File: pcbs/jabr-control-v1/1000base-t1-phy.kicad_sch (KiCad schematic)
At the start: 1 part, among them U6001 LAN8870

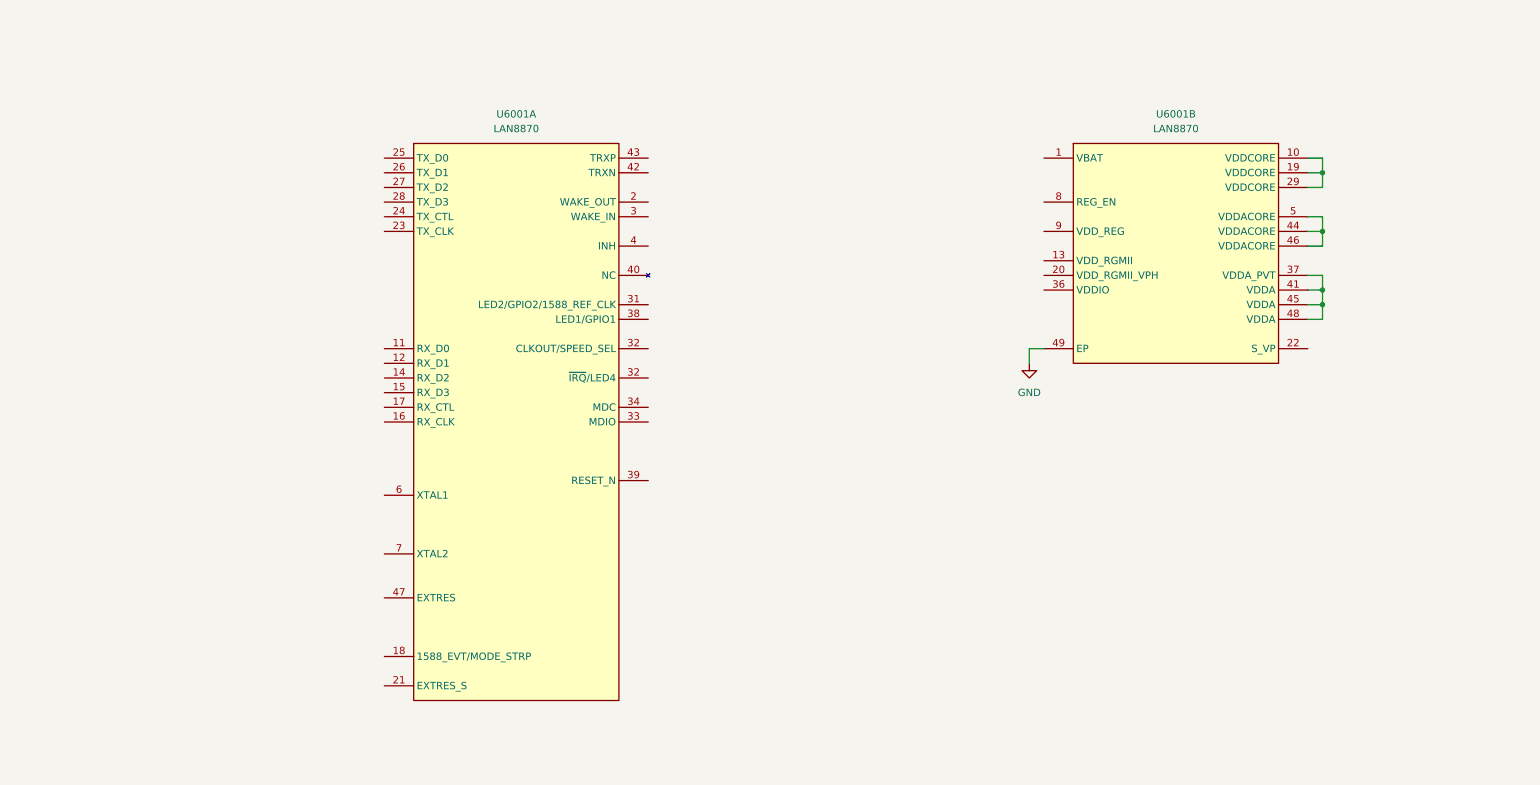
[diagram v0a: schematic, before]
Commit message: Added PCIe connections
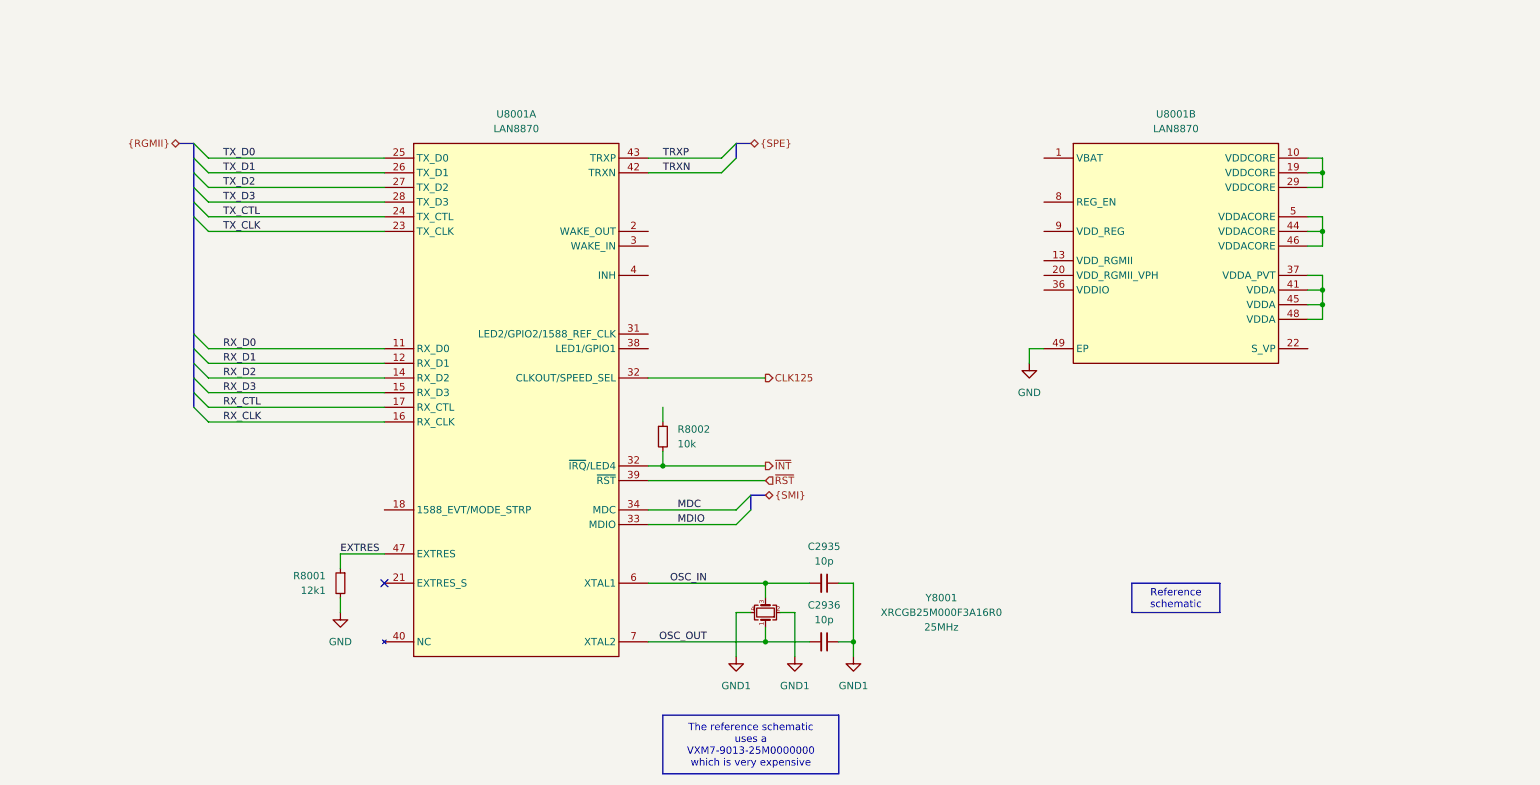
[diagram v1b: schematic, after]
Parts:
- added C2935, C2936: 10p, project_footprints:C_0402, symbol DEV:C_SMALL
- added R8001: 12k1, project_footprints:R_0402, symbol DEV:R_SMALL
- added R8002: 10k, project_footprints:R_0402, symbol DEV:R_SMALL
- added Y8001: XRCGB25M000F3A16R0, project_footprints:XRCGB25M000F3A16R0, symbol Device:Crystal_GND24_Small
- renumbered U6001 to U8001
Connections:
- net GND: now also R8001.2
- net RX_D0: now reaches U8001.11 (RX_D0)
- net RX_D1: now reaches U8001.12 (RX_D1)
- net RX_D2: now reaches U8001.14 (RX_D2)
- net RX_D3: now reaches U8001.15 (RX_D3)
- net RX_CLK: now reaches U8001.16 (RX_CLK)
- net RX_CTL: now reaches U8001.17 (RX_CTL)
- net TX_CLK: now reaches U8001.23 (TX_CLK)
- net TX_CTL: now reaches U8001.24 (TX_CTL)
- net TX_D0: now reaches U8001.25 (TX_D0)
- net TX_D1: now reaches U8001.26 (TX_D1)
- net TX_D2: now reaches U8001.27 (TX_D2)
- net TX_D3: now reaches U8001.28 (TX_D3)
- net ~{INT}: now reaches U8001.32 (~{IRQ}/LED4)
- net ~{INT}: now also R8002.2
- net MDIO: now reaches U8001.33 (MDIO)
- net MDC: now reaches U8001.34 (MDC)
- net ~{RST}: now reaches U8001.39 (~{RST})
- net TRXN: now reaches U8001.42 (TRXN)
- net TRXP: now reaches U8001.43 (TRXP)
- net EXTRES: now reaches U8001.47 (EXTRES)
- net EXTRES: now also R8001.1
- net OSC_IN: now reaches U8001.6 (XTAL1)
- net OSC_IN: now also C2935.2, Y8001.3
- net OSC_OUT: now reaches U8001.7 (XTAL2)
- net OSC_OUT: now also C2936.2, Y8001.1
- new net CLK125: U8001.32 (~{IRQ}/LED4)
- new net GND1: C2935.1, C2936.1, Y8001.2, Y8001.4
- no-connect marks 0 -> 1
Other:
- moved on the sheet: U8001A

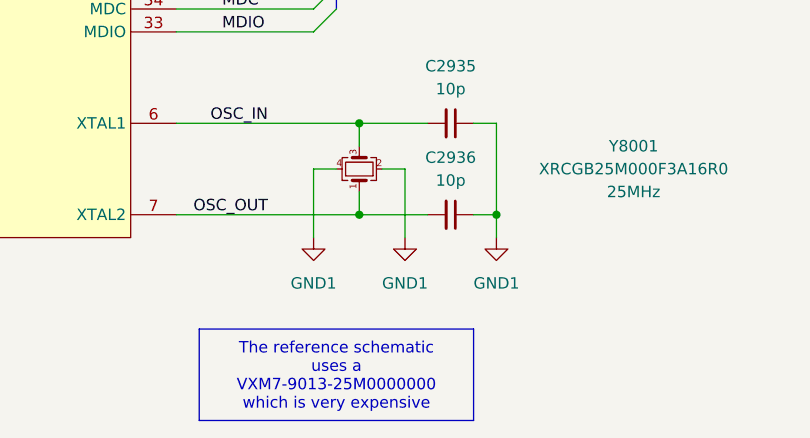
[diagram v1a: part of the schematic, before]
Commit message: Added power sheets
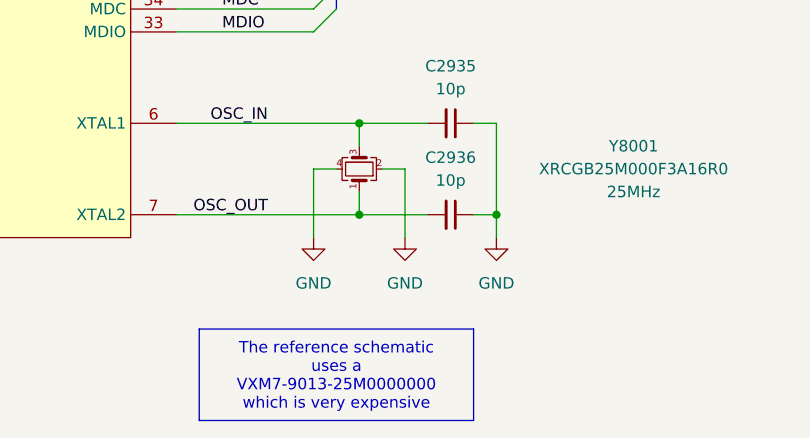
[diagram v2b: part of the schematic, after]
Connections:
- net GND1 is gone; now on net GND: C2935.1, C2936.1, Y8001.2, Y8001.4
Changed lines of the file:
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@@
 	)
 	(symbol
-		(lib_id "power:GND1")
+		(lib_id "power:GND")
 		(at 160.02 139.7 0)
 		(mirror y)
@@
 		(dnp no)
 		(fields_autoplaced yes)
-		(property "Reference" "#PWR02928"
+		(property "Reference" "#PWR2928"
 			(at 160.02 146.05 0)
 			(effects
@@
 			)
 		)
-		(property "Value" "GND1"
+		(property "Value" "GND"
 			(at 160.02 144.78 0)
 			(effects
@@
 			)
 		)
-		(property "Description" "Power symbol creates a global label with name \"GND1\" , ground"
+		(property "Description" "Power symbol creates a global label with name \"GND\" , ground"
 			(at 160.02 139.7 0)
 			(effects
@@
 			(project "jabr-control-v1"
 				(path "/f91ec272-d09a-4038-bbbb-962739a92c51/3124e188-7d93-47d9-82c9-cb765ca396d3/d93fedc6-4251-42e0-84b2-9bf0445840d2"
-					(reference "#PWR02928")
+					(reference "#PWR2928")
 					(unit 1)
 				)
@@
 	)
 	(symbol
-		(lib_id "power:GND1")
+		(lib_id "power:GND")
 		(at 149.86 139.7 0)
 		(mirror y)
@@
 		(dnp no)
 		(fields_autoplaced yes)
-		(property "Reference" "#PWR02929"
+		(property "Reference" "#PWR2929"
 			(at 149.86 146.05 0)
 			(effects
@@
 			)
 		)
-		(property "Value" "GND1"
+		(property "Value" "GND"
 			(at 149.86 144.78 0)
 			(effects
@@
 			)
 		)
-		(property "Description" "Power symbol creates a global label with name \"GND1\" , ground"
+		(property "Description" "Power symbol creates a global label with name \"GND\" , ground"
 			(at 149.86 139.7 0)
 			(effects
@@
 			(project "jabr-control-v1"
 				(path "/f91ec272-d09a-4038-bbbb-962739a92c51/3124e188-7d93-47d9-82c9-cb765ca396d3/d93fedc6-4251-42e0-84b2-9bf0445840d2"
-					(reference "#PWR02929")
+					(reference "#PWR2929")
 					(unit 1)
 				)
@@
 	)
 	(symbol
-		(lib_id "power:GND1")
+		(lib_id "power:GND")
 		(at 139.7 139.7 0)
 		(mirror y)
@@
 		(dnp no)
 		(fields_autoplaced yes)
-		(property "Reference" "#PWR02930"
+		(property "Reference" "#PWR2930"
 			(at 139.7 146.05 0)
 			(effects
@@
 			)
 		)
-		(property "Value" "GND1"
+		(property "Value" "GND"
 			(at 139.7 144.78 0)
 			(effects
@@
 			)
 		)
-		(property "Description" "Power symbol creates a global label with name \"GND1\" , ground"
+		(property "Description" "Power symbol creates a global label with name \"GND\" , ground"
 			(at 139.7 139.7 0)
 			(effects
@@
 			(project "jabr-control-v1"
 				(path "/f91ec272-d09a-4038-bbbb-962739a92c51/3124e188-7d93-47d9-82c9-cb765ca396d3/d93fedc6-4251-42e0-84b2-9bf0445840d2"
-					(reference "#PWR02930")
+					(reference "#PWR2930")
 					(unit 1)
 				)

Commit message: Worked on power and other areas of the schematic
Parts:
- added R801: 10k, project_footprints:R_0402, symbol DEV:R_SMALL
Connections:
- net GND: now also R801.2
- net +3V3_AON: now reaches U8001.1 (VBAT)
- net +1V1: now reaches U8001.10 (VDDCORE), U8001.19 (VDDCORE), U8001.29 (VDDCORE)
- net +1V1: now also U8001.44 (VDDACORE), U8001.46 (VDDACORE), U8001.5 (VDDACORE)
- net at U8001.13 (VDD_RGMII): now also U8001.20 (VDD_RGMII_VPH), U8001.36 (VDDIO)
- net REG_EN: now reaches U8001.8 (REG_EN)
- net REG_EN: now also R801.1
- net +3V3: now reaches U8001.9 (VDD_REG)
- net INH: now reaches U8001.4 (INH)

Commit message: Various small updates
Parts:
- added TP8001, TP8002: 1.5mm, TestPoint:TestPoint_Pad_D1.5mm, symbol Connector:TestPoint_Small
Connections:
- net S_VP: now reaches U8001.22 (S_VP)
- net S_VP: now also TP8001.1
- net 1588_CLK_ADJ: now reaches U8001.38 (LED1/GPIO1)
- net 1588_CLK_ADJ: now also TP8002.1
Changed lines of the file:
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@@
 		)
 	)
-	(text_box "3.3V: VDD_SYS, VBAT, \n\nVDD, VDD_REG, VDDA\n\nVDDIO, VDDIO_EDS"
+	(text_box "3.3V: VDD_SYS, VBAT, VDD, VDD_REG, VDDA\n\nVDDIO, VDDIO_EDS"
 		(exclude_from_sim no)
 		(at 198.12 104.14 0)
-		(size 22.86 12.7)
+		(size 45.72 12.7)
 		(margins 0.9525 0.9525 0.9525 0.9525)
 		(stroke
@@
 	(wire
 		(pts
+			(xy 124.46 86.36) (xy 142.24 86.36)
+		)
+		(stroke
+			(width 0)
+			(type default)
+		)
+	)
+	(wire
+		(pts
 			(xy 157.48 137.16) (xy 160.02 137.16)
 		)
@@
 	(wire
 		(pts
-			(xy 238.76 86.36) (xy 241.3 86.36)
+			(xy 238.76 86.36) (xy 254 86.36)
 		)
 		(stroke
@@
 			(width 0)
 			(type default)
+		)
+	)
+	(label "S_VP"
+		(at 241.3 86.36 0)
+		(effects
+			(font
+				(size 1.27 1.27)
+			)
+			(justify left bottom)
 		)
 	)
@@
 	(label "RX_CLK"
 		(at 50.8 99.06 0)
+		(effects
+			(font
+				(size 1.27 1.27)
+			)
+			(justify left bottom)
+		)
+	)
+	(label "1588_CLK_ADJ"
+		(at 127 86.36 0)
 		(effects
 			(font
@@
 				(path "/f91ec272-d09a-4038-bbbb-962739a92c51/3124e188-7d93-47d9-82c9-cb765ca396d3/d93fedc6-4251-42e0-84b2-9bf0445840d2"
 					(reference "#PWR0803")
+					(unit 1)
+				)
+			)
+		)
+	)
+	(symbol
+		(lib_id "Connector:TestPoint_Small")
+		(at 142.24 86.36 0)
+		(mirror y)
+		(unit 1)
+		(exclude_from_sim no)
+		(in_bom yes)
+		(on_board yes)
+		(dnp no)
+		(property "Reference" "TP8002"
+			(at 151.13 86.36 0)
+			(effects
+				(font
+					(size 1.27 1.27)
+				)
+				(justify left)
+			)
+		)
+		(property "Value" "1.5mm"
+			(at 152.4 86.36 0)
+			(effects
+				(font
+					(size 1.27 1.27)
+				)
+				(justify right)
+			)
+		)
+		(property "Footprint" "TestPoint:TestPoint_Pad_D1.5mm"
+			(at 137.16 86.36 0)
+			(effects
+				(font
+					(size 1.27 1.27)
+				)
+				(hide yes)
+			)
+		)
+		(property "Datasheet" "~"
+			(at 137.16 86.36 0)
+			(effects
+				(font
+					(size 1.27 1.27)
+				)
+				(hide yes)
+			)
+		)
+		(property "Description" "test point"
+			(at 142.24 86.36 0)
+			(effects
+				(font
+					(size 1.27 1.27)
+				)
+				(hide yes)
+			)
+		)
+		(pin "1"
+		)
+		(instances
+			(project "jabr-control-v1"
+				(path "/f91ec272-d09a-4038-bbbb-962739a92c51/3124e188-7d93-47d9-82c9-cb765ca396d3/d93fedc6-4251-42e0-84b2-9bf0445840d2"
+					(reference "TP8002")
 					(unit 1)
 				)
@@
 					(unit 1)
 				)
+			)
+		)
+	)
+	(symbol
+		(lib_id "Connector:TestPoint_Small")
+		(at 254 86.36 0)
+		(mirror y)
+		(unit 1)
+		(exclude_from_sim no)
+		(in_bom yes)
+		(on_board yes)
+		(dnp no)
+		(property "Reference" "TP8001"
+			(at 262.89 86.36 0)
+			(effects
+				(font
+					(size 1.27 1.27)
+				)
+				(justify left)
+			)
+		)
+		(property "Value" "1.5mm"
+			(at 264.16 86.36 0)
+			(effects
+				(font
+					(size 1.27 1.27)
+				)
+				(justify right)
+			)
+		)
+		(property "Footprint" "TestPoint:TestPoint_Pad_D1.5mm"
+			(at 248.92 86.36 0)
+			(effects
+				(font
+					(size 1.27 1.27)
+				)
+				(hide yes)
+			)
+		)
+		(property "Datasheet" "~"
+			(at 248.92 86.36 0)
+			(effects
+				(font
+					(size 1.27 1.27)
+				)
+				(hide yes)
+			)
+		)
+		(property "Description" "test point"
+			(at 254 86.36 0)
+			(effects
+				(font
+					(size 1.27 1.27)
+				)
+				(hide yes)
+			)
+		)
+		(pin "1"
+		)
+		(instances
+			(project "jabr-control-v1"
+				(path "/f91ec272-d09a-4038-bbbb-962739a92c51/3124e188-7d93-47d9-82c9-cb765ca396d3/d93fedc6-4251-42e0-84b2-9bf0445840d2"
+					(reference "TP8001")
+					(unit 1)
+				)

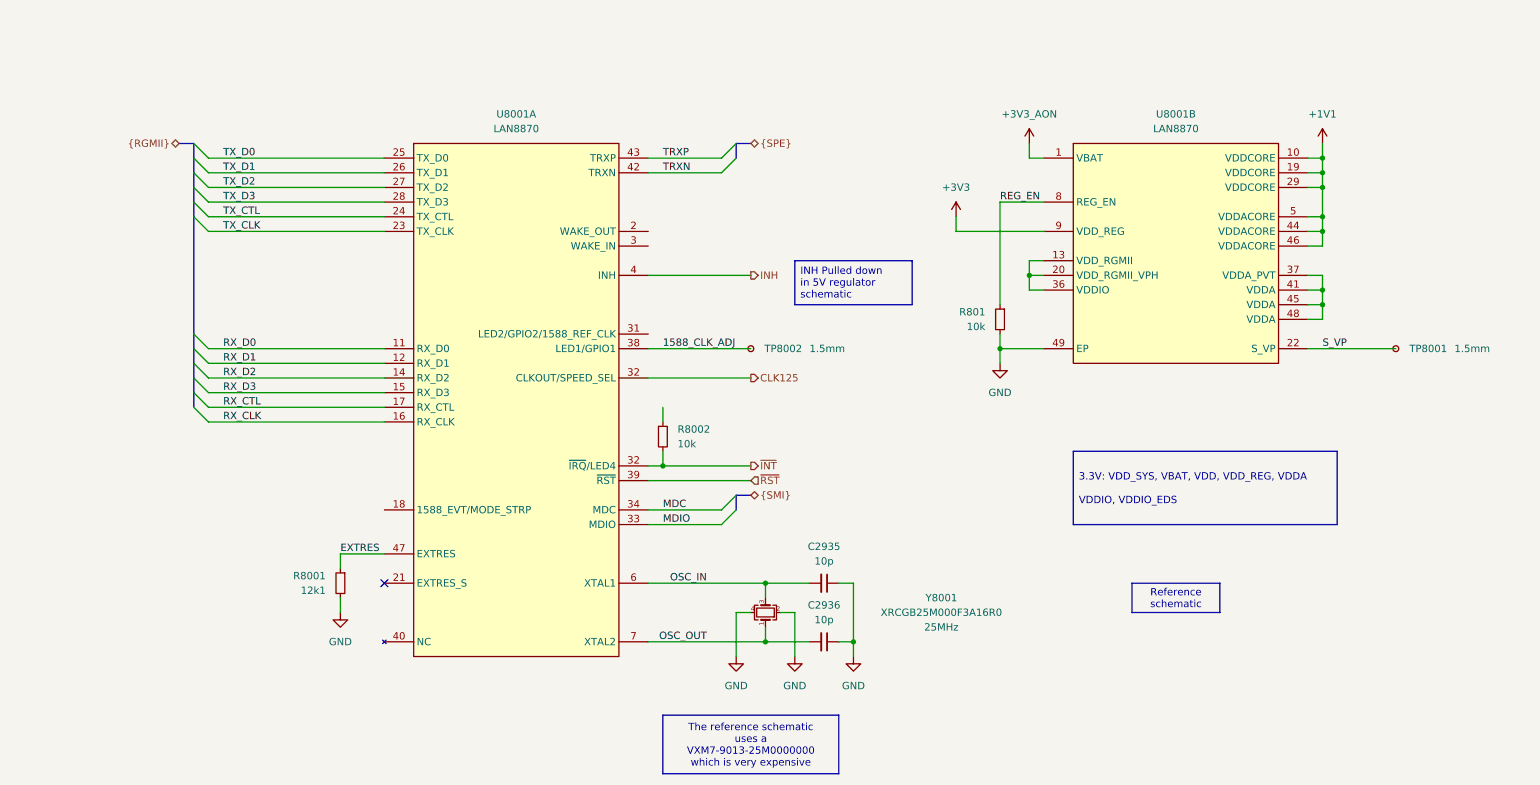
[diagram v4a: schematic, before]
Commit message: Progress on LAN7431 power
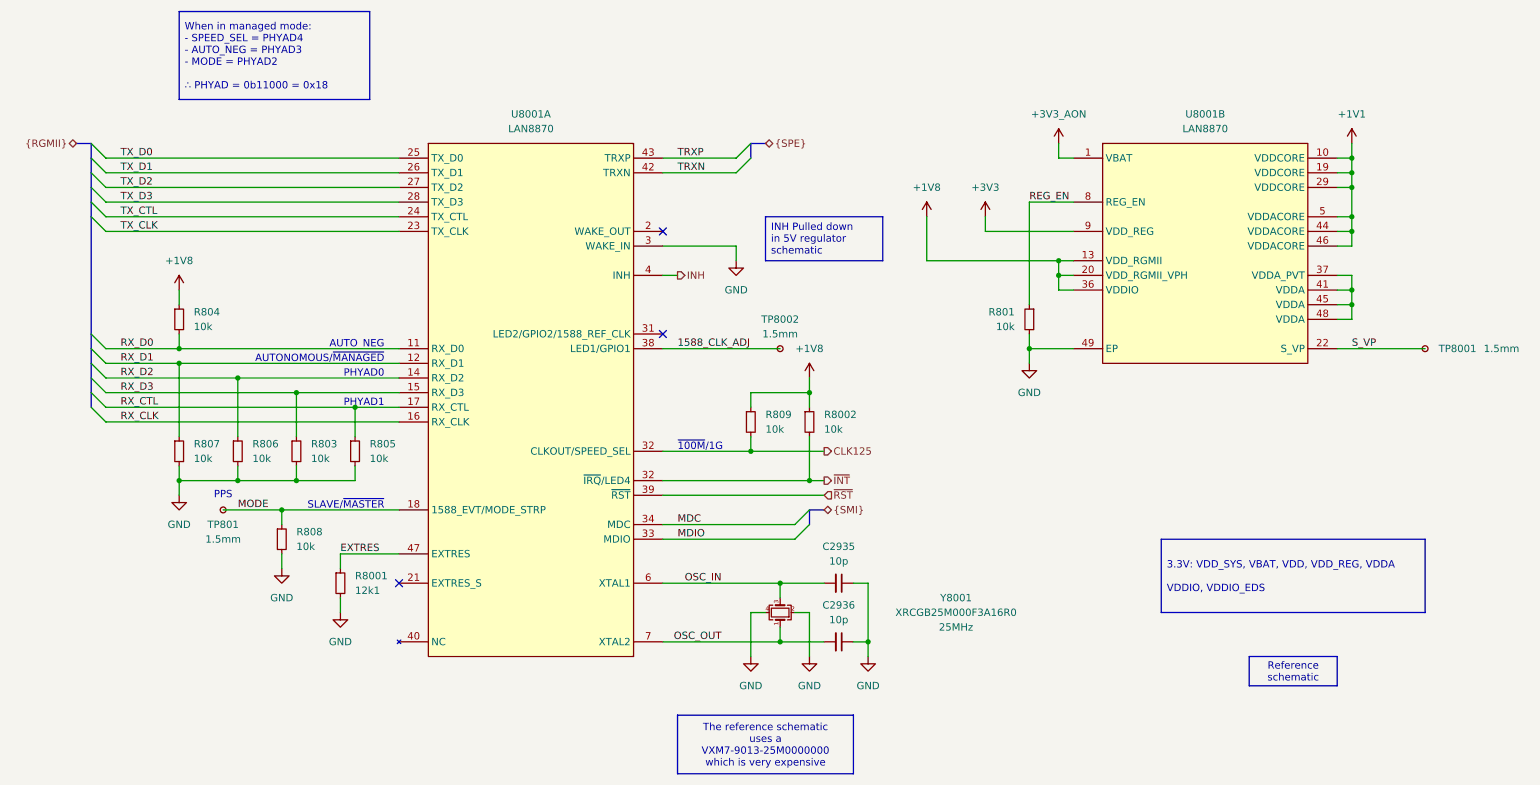
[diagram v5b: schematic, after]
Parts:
- added R803, R804, R805, R806, R807, R808, R809: 10k, project_footprints:R_0402, symbol DEV:R_SMALL
- added TP801: 1.5mm, TestPoint:TestPoint_Pad_D1.5mm, symbol Connector:TestPoint_Small
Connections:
- net CLK125: now also R809.2
- net GND: now also U8001.3 (WAKE_IN), R803.2, R805.2, R806.2, R807.2, R808.2
- net RX_CTL: now also R805.1
- net RX_D0: now also R804.2
- net RX_D1: now also R807.1
- net RX_D2: now also R806.1
- net RX_D3: now also R803.1
- net +1V8: now reaches U8001.13 (VDD_RGMII), U8001.20 (VDD_RGMII_VPH), U8001.36 (VDDIO)
- net +1V8: now also R8002.1, R804.1, R809.1
- net MODE: now reaches U8001.18 (1588_EVT/MODE_STRP)
- net MODE: now also R808.1, TP801.1
- no-connect marks 1 -> 3
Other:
- note added: "AUTONOMOUS/~{MANAGED}"
- note added: "AUTO_NEG"
- note added: "PHYAD0"
- note added: "PHYAD1"
- note added: "PPS"
- note added: "SLAVE/~{MASTER}"
- note added: "~{100M}/1G"
- moved on the sheet: C2935, C2936, R8002, R801, TP8001, TP8002, U8001A, U8001B, Y8001
